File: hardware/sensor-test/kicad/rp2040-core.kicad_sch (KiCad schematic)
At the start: 31 parts, among them J91 LOGICAL_GPIO_BREAKOUT_NOT_FIT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, J92 LOGICAL_GPIO_BREAKOUT_NOT_FIT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, J93 Conn_01x02, U1 RP2040, U2 W25Q16JVUXIQ, X2 External 3V3 from USB power s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, Y1 ABM8-272-T3

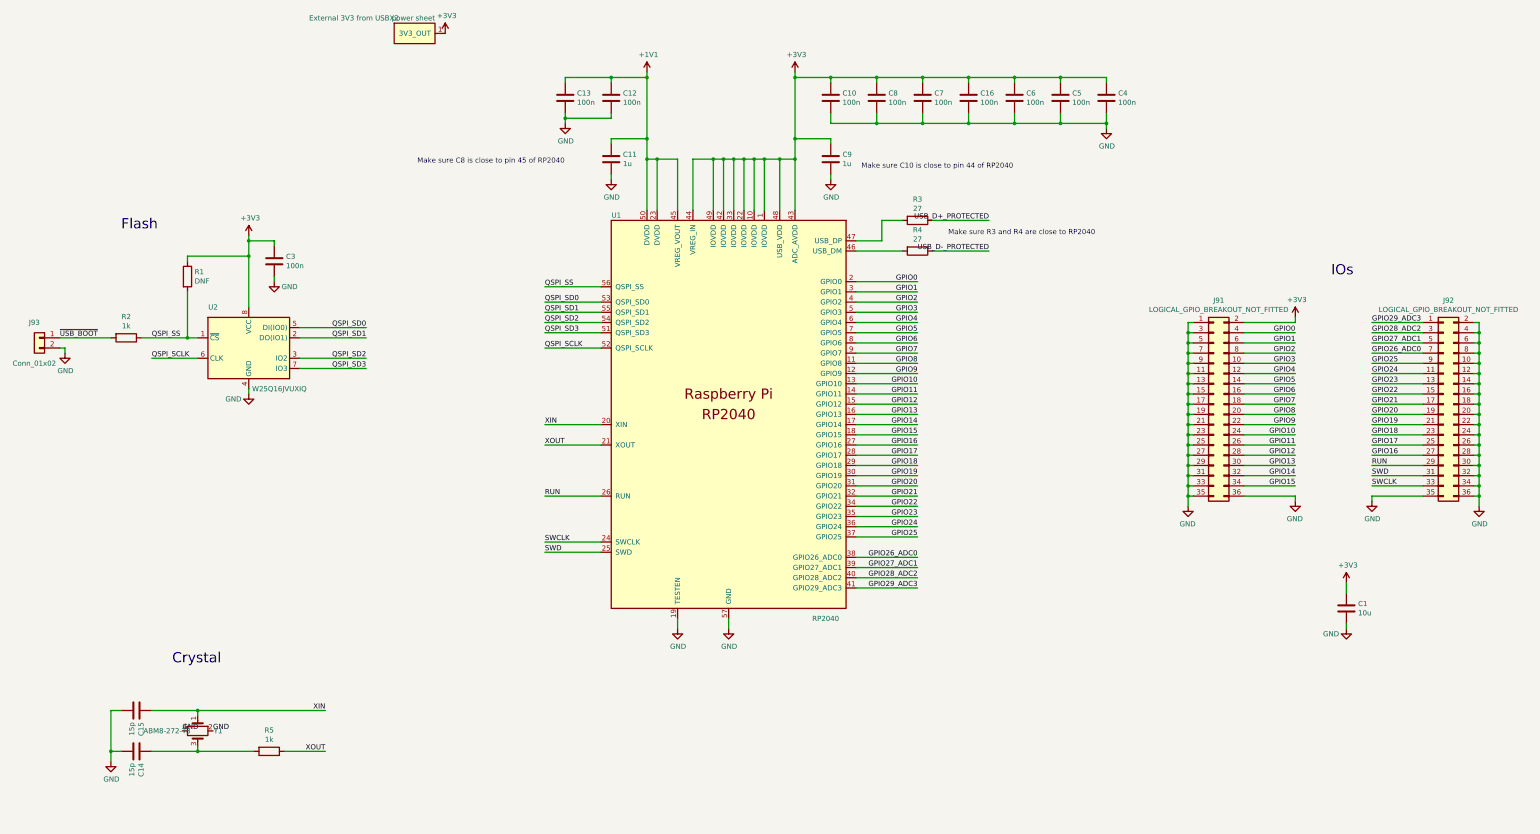
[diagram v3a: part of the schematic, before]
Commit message: Add BOOTSEL reset and SWD access to RP2040 core
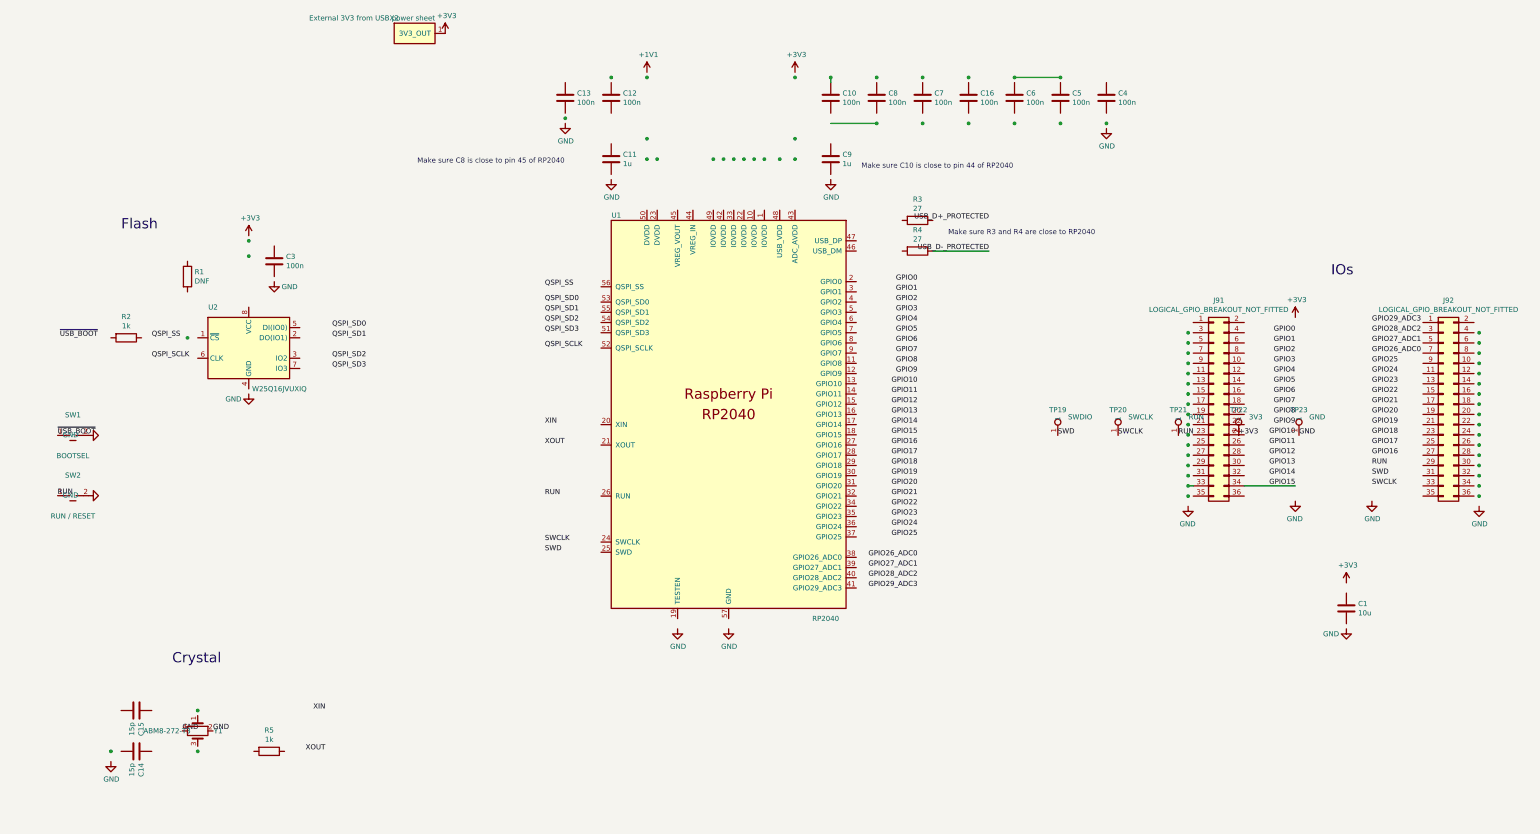
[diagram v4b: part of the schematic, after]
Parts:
- removed J93: Conn_01x02, Connector_PinHeader_2.54mm:PinHeader_1x02_P2.54mm_Vertical, symbol Connector_Generic:Conn_01x02
- added SW1: BOOTSEL, Button_Switch_SMD:SW_SPST_PTS810, symbol HEP:SW_Push
- added SW2: RUN / RESET, Button_Switch_SMD:SW_SPST_PTS810, symbol HEP:SW_Push
- added TP19: SWDIO, TestPoint:TestPoint_Pad_D1.5mm, symbol Connector:TestPoint
- added TP20: SWCLK, TestPoint:TestPoint_Pad_D1.5mm, symbol Connector:TestPoint
- added TP21: RUN, TestPoint:TestPoint_Pad_D1.5mm, symbol Connector:TestPoint
- added TP22: 3V3, TestPoint:TestPoint_Pad_D1.5mm, symbol Connector:TestPoint
- added TP23: GND, TestPoint:TestPoint_Pad_D1.5mm, symbol Connector:TestPoint
- R1, R2: footprint Capacitor_SMD:C_0402_1005Metric -> Resistor_SMD:R_0603_1608Metric
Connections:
- net +1V1: no longer C11.1, C12.1, C13.1, U1.23 (DVDD), U1.45 (VREG_VOUT), U1.50 (DVDD)
- net +3V3: now also TP22.1; no longer C1.1, C10.1, C16.1, C3.1, C4.1, C5.1, C6.1, C7.1, C8.1, C9.1, J91.2 (Pin_2), R1.1, U1.1 (IOVDD), U1.10 (IOVDD), U1.22 (IOVDD), U1.33 (IOVDD), U1.42 (IOVDD), U1.43 (ADC_AVDD), U1.44 (VREG_IN), U1.48 (USB_VDD), U1.49 (IOVDD), U2.8 (VCC)
- net GND: now also SW1.2, SW2.2, TP23.1; no longer C1.2, C10.2, C11.2, C12.2, C13.2, C14.2, C15.2, C16.2, C3.2, C4.2, C5.2, C6.2, C7.2, C8.2, C9.2, J91.1 (Pin_1), J91.11 (Pin_11), J91.13 (Pin_13), J91.15 (Pin_15), J91.17 (Pin_17), J91.19 (Pin_19), J91.21 (Pin_21), J91.23 (Pin_23), J91.25 (Pin_25), J91.27 (Pin_27), J91.29 (Pin_29), J91.3 (Pin_3), J91.31 (Pin_31), J91.33 (Pin_33), J91.35 (Pin_35), J91.36 (Pin_36), J91.5 (Pin_5), J91.7 (Pin_7), J91.9 (Pin_9), J92.10 (Pin_10), J92.12 (Pin_12), J92.14 (Pin_14), J92.16 (Pin_16), J92.18 (Pin_18), J92.2 (Pin_2), J92.20 (Pin_20), J92.22 (Pin_22), J92.24 (Pin_24), J92.26 (Pin_26), J92.28 (Pin_28), J92.30 (Pin_30), J92.32 (Pin_32), J92.34 (Pin_34), J92.35 (Pin_35), J92.36 (Pin_36), J92.4 (Pin_4), J92.6 (Pin_6), J92.8 (Pin_8), U1.19 (TESTEN), U1.57 (GND), U2.4 (GND)
- net GPIO0: no longer J91.4 (Pin_4), U1.2 (GPIO0)
- net GPIO1: no longer J91.6 (Pin_6), U1.3 (GPIO1)
- net GPIO10: no longer J91.24 (Pin_24), U1.13 (GPIO10)
- net GPIO11: no longer J91.26 (Pin_26), U1.14 (GPIO11)
- net GPIO12: no longer J91.28 (Pin_28), U1.15 (GPIO12)
- net GPIO13: no longer J91.30 (Pin_30), U1.16 (GPIO13)
- net GPIO14: no longer J91.32 (Pin_32), U1.17 (GPIO14)
- net GPIO15: no longer U1.18 (GPIO15)
- net GPIO16: no longer J92.27 (Pin_27), U1.27 (GPIO16)
- net GPIO17: no longer J92.25 (Pin_25), U1.28 (GPIO17)
- net GPIO18: no longer J92.23 (Pin_23), U1.29 (GPIO18)
- net GPIO19: no longer J92.21 (Pin_21), U1.30 (GPIO19)
- net GPIO2: no longer J91.8 (Pin_8), U1.4 (GPIO2)
- net GPIO20: no longer J92.19 (Pin_19), U1.31 (GPIO20)
- net GPIO21: no longer J92.17 (Pin_17), U1.32 (GPIO21)
- net GPIO22: no longer J92.15 (Pin_15), U1.34 (GPIO22)
- net GPIO23: no longer J92.13 (Pin_13), U1.35 (GPIO23)
- net GPIO24: no longer J92.11 (Pin_11), U1.36 (GPIO24)
- net GPIO25: no longer J92.9 (Pin_9), U1.37 (GPIO25)
- net GPIO26_ADC0: no longer J92.7 (Pin_7), U1.38 (GPIO26_ADC0)
- net GPIO27_ADC1: no longer J92.5 (Pin_5), U1.39 (GPIO27_ADC1)
- net GPIO28_ADC2: no longer J92.3 (Pin_3), U1.40 (GPIO28_ADC2)
- net GPIO29_ADC3: no longer J92.1 (Pin_1), U1.41 (GPIO29_ADC3)
- net GPIO3: no longer J91.10 (Pin_10), U1.5 (GPIO3)
- net GPIO4: no longer J91.12 (Pin_12), U1.6 (GPIO4)
- net GPIO5: no longer J91.14 (Pin_14), U1.7 (GPIO5)
- net GPIO6: no longer J91.16 (Pin_16), U1.8 (GPIO6)
- net GPIO7: no longer J91.18 (Pin_18), U1.9 (GPIO7)
- net GPIO8: no longer J91.20 (Pin_20), U1.11 (GPIO8)
- net GPIO9: no longer J91.22 (Pin_22), U1.12 (GPIO9)
- net QSPI_SCLK: no longer U1.52 (QSPI_SCLK), U2.6 (CLK)
- net QSPI_SD0: no longer U1.53 (QSPI_SD0), U2.5 (DI(IO0))
- net QSPI_SD1: no longer U1.55 (QSPI_SD1), U2.2 (DO(IO1))
- net QSPI_SD2: no longer U1.54 (QSPI_SD2), U2.3 (IO2)
- net QSPI_SD3: no longer U1.51 (QSPI_SD3), U2.7 (IO3)
- net QSPI_SS: no longer R1.2, R2.1, U1.56 (QSPI_SS), U2.1 (~{CS})
- net RUN: now also SW2.1, TP21.1; no longer J92.29 (Pin_29), U1.26 (RUN)
- net SWCLK: now also TP20.1; no longer J92.33 (Pin_33), U1.24 (SWCLK)
- net SWD: now also TP19.1; no longer J92.31 (Pin_31), U1.25 (SWD)
- net USB_D+_PROTECTED: no longer R3.1
- net XIN: no longer C15.1, U1.20 (XIN), Y1.1 (XTAL1)
- net XOUT: no longer R5.1, U1.21 (XOUT)
- net ~{USB_BOOT}: now also SW1.1; no longer R2.2
- net at U1.46 (USB_DM): no longer R4.2
- net at U1.47 (USB_DP): no longer R3.2
- now unconnected: C14.1, R5.2, Y1.3 (XTAL2)

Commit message: Normalize eval-board references and remove legacy breakouts
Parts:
- removed H90, H91, H92, H93: MountingHole, MountingHole:MountingHole_2.7mm_M2.5, symbol Mechanical:MountingHole
- removed J91, J92: LOGICAL_GPIO_BREAKOUT_NOT_FITTED, Connector_PinHeader_2.54mm:PinHeader_2x18_P2.54mm_Vertical, symbol Connector_Generic:Conn_02x18_Odd_Even
- renumbered C1 to C26, R1 to R8, R2 to R9

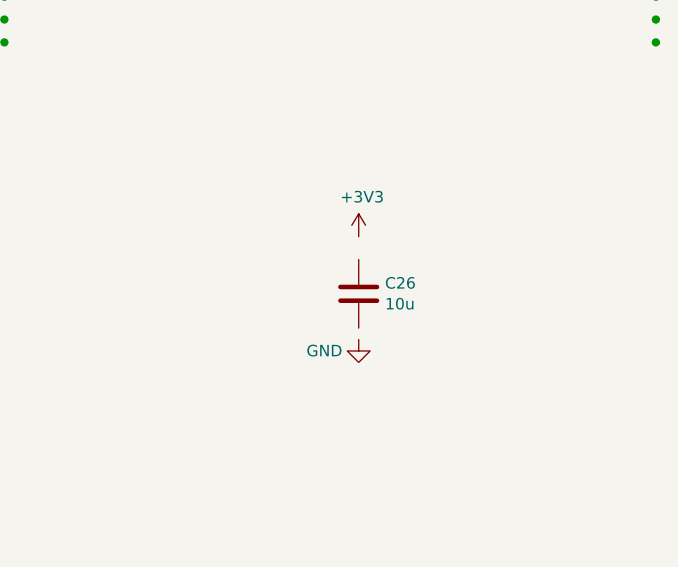
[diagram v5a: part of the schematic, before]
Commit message: Use contiguous eval-board capacitor references
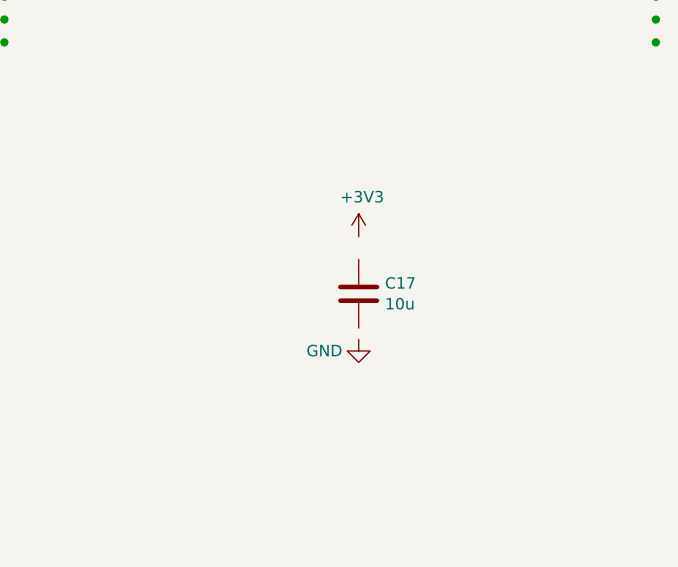
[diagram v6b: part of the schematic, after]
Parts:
- renumbered C26 to C17
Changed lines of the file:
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@@
   (symbol (lib_id "Device:C") (at 351.79 193.04 0) (unit 1)
     (in_bom yes) (on_board yes) (dnp no)
-    (property "Reference" "C26" (at 354.711 191.8716 0)
+    (property "Reference" "C17" (at 354.711 191.8716 0)
       (effects (font (size 1.27 1.27)) (justify left))
     )
@@
       (project "rp2040-core"
         (path "/0b572f4d-42c2-4e67-a259-3bf815f1855a"
-          (reference "C26") (unit 1)
+          (reference "C17") (unit 1)
         )
       )

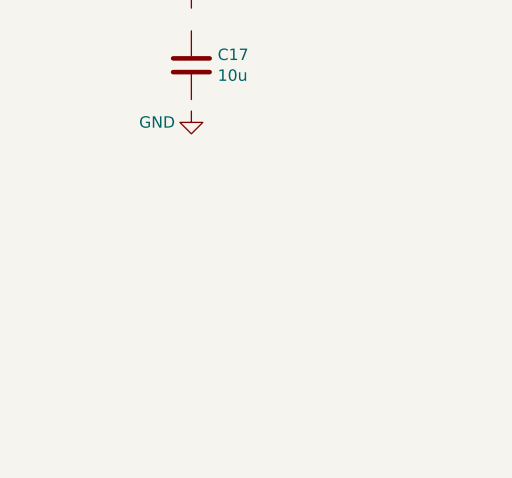
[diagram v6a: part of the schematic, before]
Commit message: Add GPIO11 status LED
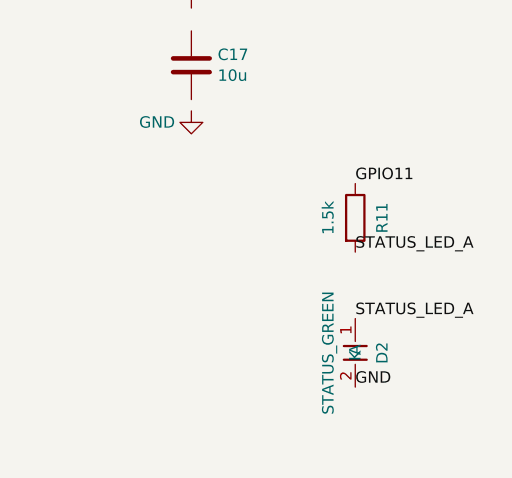
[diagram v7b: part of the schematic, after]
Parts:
- added D2: STATUS_GREEN, LED_SMD:LED_0603_1608Metric, symbol HEP:LED
- added R11: 1.5k, Resistor_SMD:R_0603_1608Metric, symbol Device:R
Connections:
- net GND: now also D2.2 (A)
- net GPIO11: now also R11.1
- new net STATUS_LED_A: D2.1 (K), R11.2
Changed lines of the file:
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@@
     (effects (font (size 1.27 1.27)) (justify left bottom))
   )
+  (symbol (lib_id "Device:R") (at 370 210 0) (unit 1)
+    (in_bom yes) (on_board yes) (dnp no)
+    (property "Reference" "R11" (at 373 210 90) (effects (font (size 1.27 1.27))))
+    (property "Value" "1.5k" (at 367 210 90) (effects (font (size 1.27 1.27))))
+    (property "Footprint" "Resistor_SMD:R_0603_1608Metric" (at 370 210 0) (effects (font (size 1.27 1.27)) hide))
+    (property "Datasheet" "~" (at 370 210 0) (effects (font (size 1.27 1.27)) hide))
+    (pin "1")
+    (pin "2")
+    (instances (project "rp2040-core" (path "/0b572f4d-42c2-4e67-a259-3bf815f1855a" (reference "R11") (unit 1))))
+  )
+  (label "GPIO11" (at 370 206.19 0) (effects (font (size 1.27 1.27)) (justify left bottom)))
+  (label "STATUS_LED_A" (at 370 213.81 0) (effects (font (size 1.27 1.27)) (justify left bottom)))
+  (symbol (lib_id "HEP:LED") (at 370 225 0) (unit 1)
+    (in_bom yes) (on_board yes) (dnp no)
+    (property "Reference" "D2" (at 373 225 90) (effects (font (size 1.27 1.27))))
+    (property "Value" "STATUS_GREEN" (at 367 225 90) (effects (font (size 1.27 1.27))))
+    (property "Footprint" "LED_SMD:LED_0603_1608Metric" (at 370 225 0) (effects (font (size 1.27 1.27)) hide))
+    (property "Datasheet" "~" (at 370 225 0) (effects (font (size 1.27 1.27)) hide))
+    (pin "1")
+    (pin "2")
+    (instances (project "rp2040-core" (path "/0b572f4d-42c2-4e67-a259-3bf815f1855a" (reference "D2") (unit 1))))
+  )
+  (label "STATUS_LED_A" (at 370 221.19 0) (effects (font (size 1.27 1.27)) (justify left bottom)))
+  (label "GND" (at 370 228.81 0) (effects (font (size 1.27 1.27)) (justify left bottom)))
   (sheet_instances
     (path "/" (page "1"))
